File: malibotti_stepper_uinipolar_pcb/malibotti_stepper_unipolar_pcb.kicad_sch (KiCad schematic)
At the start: 34 parts, among them J1 Stepper 1, J2 Stepper 2, J3 Servo, J4 I2C, J5 USB_C_Receptacle_USB2.0_16P, J6 Serial, SW1 RST, SW2 MicroSwitchLeft, SW3 MicroSwitchRight, SW8 BTN, U1 TBD62783A, U3 AMS1117, U5 ESP32-S3-MINI-1

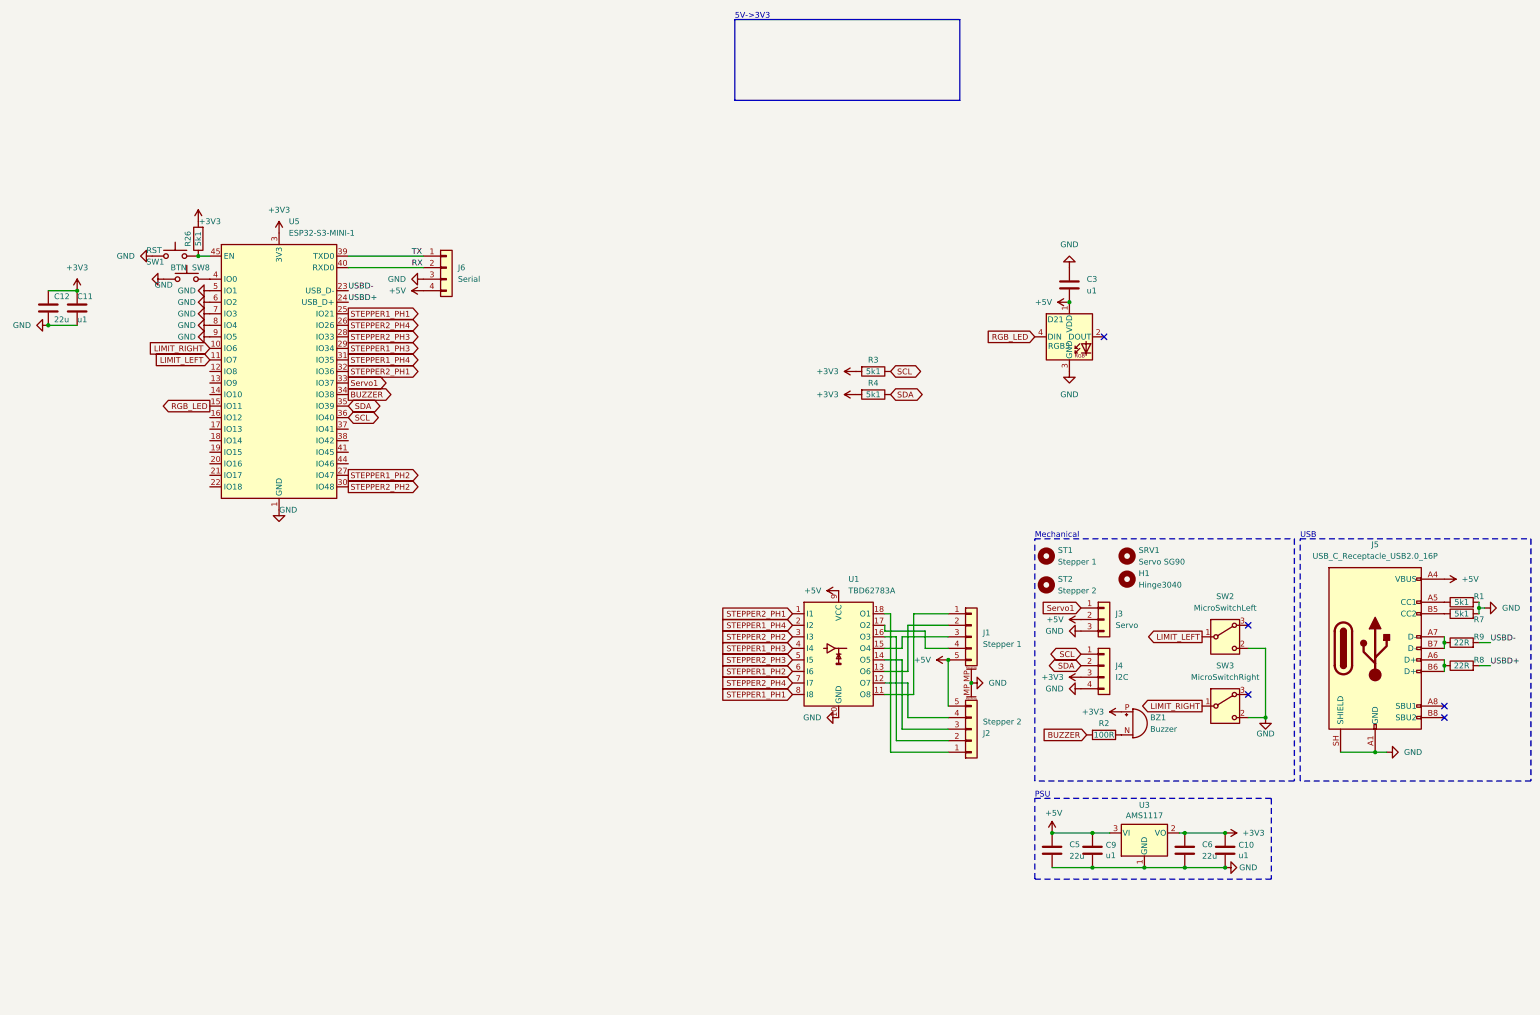
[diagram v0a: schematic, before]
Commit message: WebControlled Malibotti with working steppers
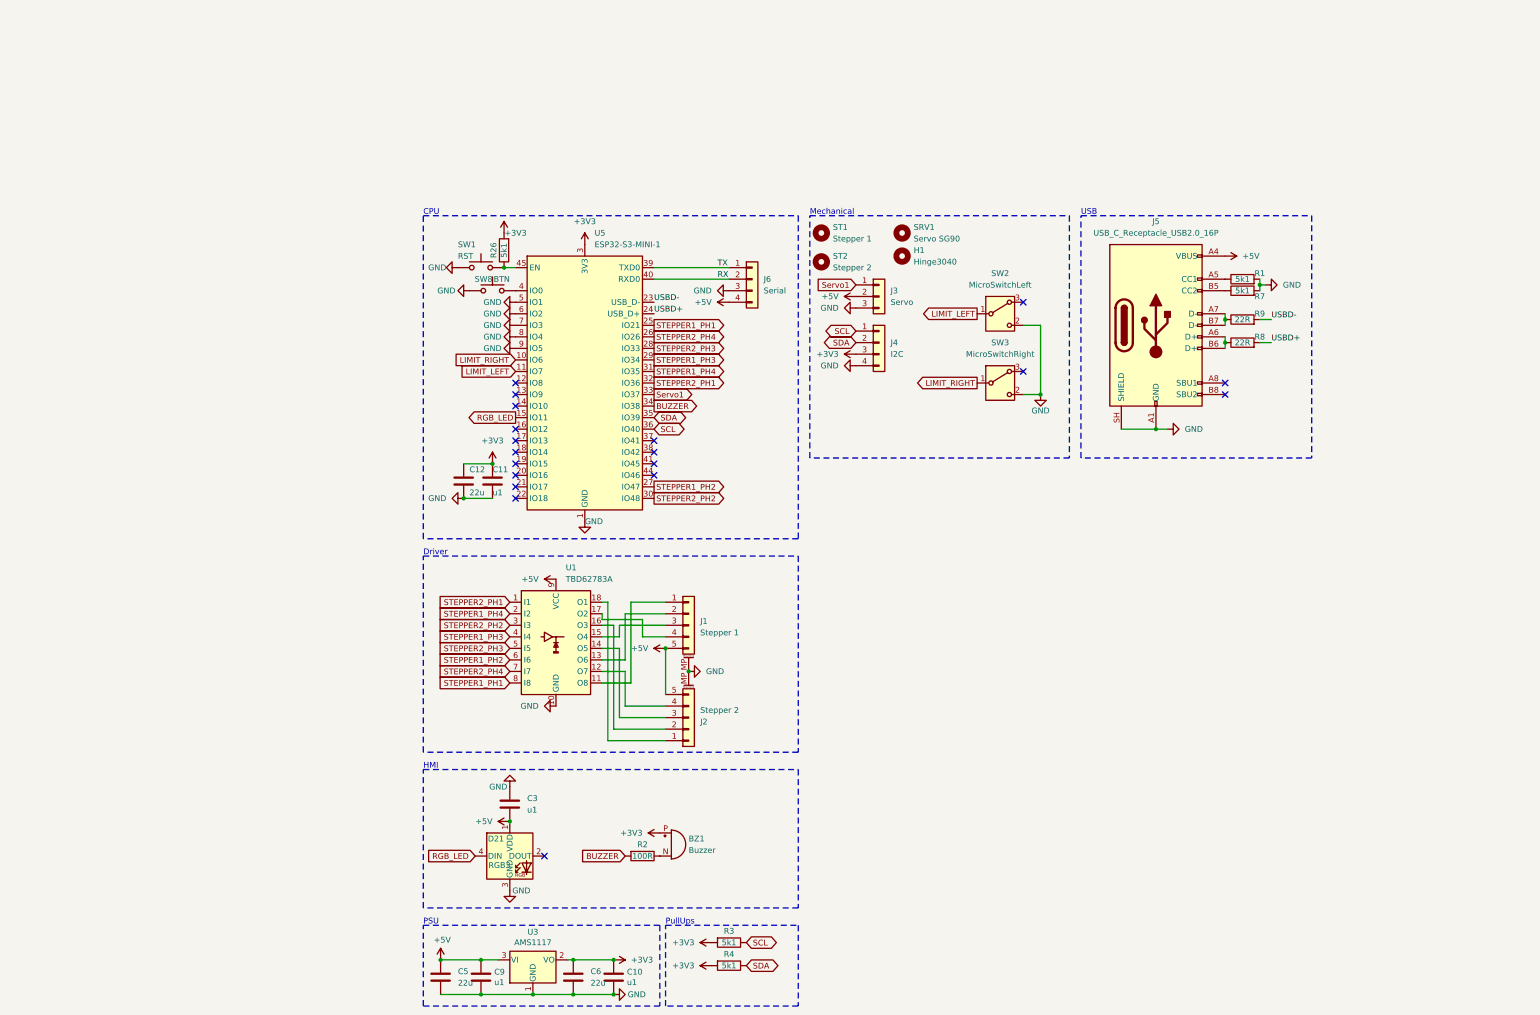
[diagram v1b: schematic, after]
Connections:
- no-connect marks 5 -> 19
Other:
- note added: "CPU"
- note added: "Driver"
- note added: "HMI"
- note added: "PullUps"
- note removed: "5V->3V3"
- moved on the sheet: BZ1, C10, C11, C12, C3, C5, C6, C9, D21, H1, J1, J2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

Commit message: Varions
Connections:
- net +5V: no longer J1.5 (Pin_5), J2.5 (Pin_5)
- net GND: now also J1.1 (Pin_1), J2.1 (Pin_1)
- net at U1.18 (O1): now also J2.5 (Pin_5); no longer J2.1 (Pin_1)
- net at J2.2 (Pin_2): now also U1.12 (O7); no longer U1.16 (O3)
- net at J2.4 (Pin_4): now also U1.16 (O3); no longer U1.12 (O7)
- net at U1.11 (O8): now also J1.5 (Pin_5); no longer J1.1 (Pin_1)
- net at U1.13 (O6): now also J1.4 (Pin_4); no longer J1.2 (Pin_2)
- net at U1.17 (O2): now also J1.2 (Pin_2); no longer J1.4 (Pin_4)
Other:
- moved on the sheet: J1
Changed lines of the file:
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@@
 	)
 	(junction
-		(at 67.31 110.49)
-		(diameter 0)
-		(color 0 0 0 0)
-	)
-	(junction
 		(at 33.02 148.59)
 		(diameter 0)
@@
 	)
 	(junction
-		(at 55.88 179.07)
+		(at 67.31 115.57)
 		(diameter 0)
 		(color 0 0 0 0)
 	)
 	(junction
-		(at 198.12 30.48)
+		(at 55.88 179.07)
 		(diameter 0)
 		(color 0 0 0 0)
 	)
 	(junction
-		(at 72.39 115.57)
+		(at 198.12 30.48)
 		(diameter 0)
 		(color 0 0 0 0)
@@
 	(wire
 		(pts
-			(xy 67.31 128.27) (xy 55.88 128.27)
+			(xy 67.31 124.46) (xy 55.88 124.46)
 		)
 		(stroke
@@
 	(wire
 		(pts
-			(xy 55.88 128.27) (xy 55.88 105.41)
+			(xy 55.88 124.46) (xy 55.88 105.41)
 		)
 		(stroke
@@
 	(wire
 		(pts
-			(xy 57.15 125.73) (xy 57.15 110.49)
+			(xy 57.15 121.92) (xy 57.15 110.49)
 		)
 		(stroke
@@
 	(wire
 		(pts
-			(xy 67.31 130.81) (xy 54.61 130.81)
+			(xy 67.31 127) (xy 54.61 127)
 		)
 		(stroke
@@
 	(wire
 		(pts
+			(xy 67.31 115.57) (xy 67.31 116.84)
+		)
+		(stroke
+			(width 0)
+			(type default)
+		)
+	)
+	(wire
+		(pts
 			(xy 58.42 102.87) (xy 58.42 113.03)
 		)
@@
 	(wire
 		(pts
-			(xy 54.61 130.81) (xy 54.61 100.33)
+			(xy 54.61 127) (xy 54.61 100.33)
 		)
 		(stroke
@@
 	(wire
 		(pts
-			(xy 67.31 110.49) (xy 67.31 120.65)
+			(xy 67.31 110.49) (xy 67.31 115.57)
 		)
 		(stroke
@@
 	(wire
 		(pts
-			(xy 58.42 123.19) (xy 58.42 115.57)
+			(xy 58.42 119.38) (xy 58.42 115.57)
 		)
 		(stroke
@@
 	(wire
 		(pts
-			(xy 67.31 125.73) (xy 57.15 125.73)
+			(xy 67.31 121.92) (xy 57.15 121.92)
 		)
 		(stroke
@@
 	(wire
 		(pts
-			(xy 67.31 123.19) (xy 58.42 123.19)
+			(xy 67.31 119.38) (xy 58.42 119.38)
 		)
 		(stroke
@@
 	)
 	(symbol
-		(lib_id "power:+5V")
-		(at 67.31 110.49 90)
-		(unit 1)
-		(body_style 1)
-		(exclude_from_sim no)
-		(in_bom yes)
-		(on_board yes)
-		(in_pos_files yes)
-		(dnp no)
-		(fields_autoplaced yes)
-		(property "Reference" "#PWR048"
-			(at 71.12 110.49 0)
-			(hide yes)
-			(show_name no)
-			(do_not_autoplace no)
-			(effects
-				(font
-					(size 1.27 1.27)
-				)
-			)
-		)
-		(property "Value" "+5V"
-			(at 63.5 110.4899 90)
-			(show_name no)
-			(do_not_autoplace no)
-			(effects
-				(font
-					(size 1.27 1.27)
-				)
-				(justify left)
-			)
-		)
-		(property "Footprint" ""
-			(at 67.31 110.49 0)
-			(hide yes)
-			(show_name no)
-			(do_not_autoplace no)
-			(effects
-				(font
-					(size 1.27 1.27)
-				)
-			)
-		)
-		(property "Datasheet" ""
-			(at 67.31 110.49 0)
-			(hide yes)
-			(show_name no)
-			(do_not_autoplace no)
-			(effects
-				(font
-					(size 1.27 1.27)
-				)
-			)
-		)
-		(property "Description" "Power symbol creates a global label with name \"+5V\""
-			(at 67.31 110.49 0)
-			(hide yes)
-			(show_name no)
-			(do_not_autoplace no)
-			(effects
-				(font
-					(size 1.27 1.27)
-				)
-			)
-		)
-		(pin "1"
-		)
-		(instances
-			(project "malibotti_stepper_unipolar_pcb"
-				(path "/e3c0928e-588c-4cab-a021-dc1d90fa1136"
-					(reference "#PWR048")
-					(unit 1)
-				)
-			)
-		)
-	)
-	(symbol
 		(lib_id "Connector_Generic:Conn_01x04")
 		(at 86.36 29.21 0)
@@
 	(symbol
 		(lib_id "Connector_Generic_MountingPin:Conn_01x05_MountingPin")
-		(at 72.39 125.73 0)
-		(mirror x)
+		(at 72.39 121.92 0)
 		(unit 1)
 		(body_style 1)
@@
 		(dnp no)
 		(property "Reference" "J2"
-			(at 74.93 126.6445 0)
+			(at 74.93 121.0055 0)
 			(show_name no)
 			(do_not_autoplace no)
@@
 		)
 		(property "Value" "Stepper 2"
-			(at 74.93 124.1045 0)
+			(at 74.93 123.5455 0)
 			(show_name no)
 			(do_not_autoplace no)
@@
 		)
 		(property "Footprint" "liebler_CONN:JST_XH_5P_SMD"
-			(at 72.39 125.73 0)
+			(at 72.39 121.92 0)
 			(hide yes)
 			(show_name no)
@@
 		)
 		(property "Datasheet" ""
-			(at 72.39 125.73 0)
+			(at 72.39 121.92 0)
 			(hide yes)
 			(show_name no)
@@
 		)
 		(property "Description" "Generic connectable mounting pin connector, single row, 01x05, script generated (kicad-library-utils/schlib/autogen/connector/)"
-			(at 72.39 125.73 0)
+			(at 72.39 121.92 0)
 			(hide yes)
 			(show_name no)
@@
 	)
 	(symbol
+		(lib_id "power:GND")
+		(at 72.39 132.08 90)
+		(unit 1)
+		(body_style 1)
+		(exclude_from_sim no)
+		(in_bom yes)
+		(on_board yes)
+		(in_pos_files yes)
+		(dnp no)
+		(fields_autoplaced yes)
+		(property "Reference" "#PWR053"
+			(at 78.74 132.08 0)
+			(hide yes)
+			(show_name no)
+			(do_not_autoplace no)
+			(effects
+				(font
+					(size 1.27 1.27)
+				)
+			)
+		)
+		(property "Value" "GND"
+			(at 76.2 132.0799 90)
+			(show_name no)
+			(do_not_autoplace no)
+			(effects
+				(font
+					(size 1.27 1.27)
+				)
+				(justify right)
+			)
+		)
+		(property "Footprint" ""
+			(at 72.39 132.08 0)
+			(hide yes)
+			(show_name no)
+			(do_not_autoplace no)
+			(effects
+				(font
+					(size 1.27 1.27)
+				)
+			)
+		)
+		(property "Datasheet" ""
+			(at 72.39 132.08 0)
+			(hide yes)
+			(show_name no)
+			(do_not_autoplace no)
+			(effects
+				(font
+					(size 1.27 1.27)
+				)
+			)
+		)
+		(property "Description" "Power symbol creates a global label with name \"GND\" , ground"
+			(at 72.39 132.08 0)
+			(hide yes)
+			(show_name no)
+			(do_not_autoplace no)
+			(effects
+				(font
+					(size 1.27 1.27)
+				)
+			)
+		)
+		(pin "1"
+		)
+		(instances
+			(project "malibotti_stepper_unipolar_pcb"
+				(path "/e3c0928e-588c-4cab-a021-dc1d90fa1136"
+					(reference "#PWR053")
+					(unit 1)
+				)
+			)
+		)
+	)
+	(symbol
 		(lib_id "Device:C")
 		(at 46.99 182.88 0)
@@
 		(lib_id "Connector_Generic_MountingPin:Conn_01x05_MountingPin")
 		(at 72.39 105.41 0)
+		(mirror x)
 		(unit 1)
 		(body_style 1)
@@
 		(in_pos_files yes)
 		(dnp no)
-		(fields_autoplaced yes)
 		(property "Reference" "J1"
-			(at 74.93 104.4955 0)
+			(at 74.93 106.3245 0)
 			(show_name no)
 			(do_not_autoplace no)
@@
 		)
 		(property "Value" "Stepper 1"
-			(at 74.93 107.0355 0)
+			(at 74.93 103.7845 0)
 			(show_name no)
 			(do_not_autoplace no)
@@
 	(symbol
 		(lib_id "power:GND")
+		(at 72.39 95.25 90)
+		(unit 1)
+		(body_style 1)
+		(exclude_from_sim no)
+		(in_bom yes)
+		(on_board yes)
+		(in_pos_files yes)
+		(dnp no)
+		(fields_autoplaced yes)
+		(property "Reference" "#PWR050"
+			(at 78.74 95.25 0)
+			(hide yes)
+			(show_name no)
+			(do_not_autoplace no)
+			(effects
+				(font
+					(size 1.27 1.27)
+				)
+			)
+		)
+		(property "Value" "GND"
+			(at 76.2 95.2499 90)
+			(show_name no)
+			(do_not_autoplace no)
+			(effects
+				(font
+					(size 1.27 1.27)
+				)
+				(justify right)
+			)
+		)
+		(property "Footprint" ""
+			(at 72.39 95.25 0)
+			(hide yes)
+			(show_name no)
+			(do_not_autoplace no)
+			(effects
+				(font
+					(size 1.27 1.27)
+				)
+			)
+		)
+		(property "Datasheet" ""
+			(at 72.39 95.25 0)
+			(hide yes)
+			(show_name no)
+			(do_not_autoplace no)
+			(effects
+				(font
+					(size 1.27 1.27)
+				)
+			)
+		)
+		(property "Description" "Power symbol creates a global label with name \"GND\" , ground"
+			(at 72.39 95.25 0)
+			(hide yes)
+			(show_name no)
+			(do_not_autoplace no)
+			(effects
+				(font
+					(size 1.27 1.27)
+				)
+			)
+		)
+		(pin "1"
+		)
+		(instances
+			(project "malibotti_stepper_unipolar_pcb"
+				(path "/e3c0928e-588c-4cab-a021-dc1d90fa1136"
+					(reference "#PWR050")
+					(unit 1)
+				)
+			)
+		)
+	)
+	(symbol
+		(lib_id "power:GND")
 		(at 21.59 26.67 270)
 		(unit 1)
@@
 	(symbol
 		(lib_id "power:GND")
-		(at 72.39 115.57 90)
+		(at 67.31 115.57 270)
 		(unit 1)
 		(body_style 1)
@@
 		(fields_autoplaced yes)
 		(property "Reference" "#PWR049"
-			(at 78.74 115.57 0)
+			(at 60.96 115.57 0)
 			(hide yes)
 			(show_name no)
@@
 		)
 		(property "Value" "GND"
-			(at 76.2 115.5699 90)
+			(at 66.04 111.76 90)
 			(show_name no)
 			(do_not_autoplace no)
@@
 					(size 1.27 1.27)
 				)
-				(justify right)
 			)
 		)
 		(property "Footprint" ""
-			(at 72.39 115.57 0)
+			(at 67.31 115.57 0)
 			(hide yes)
 			(show_name no)
@@
 		)
 		(property "Datasheet" ""
-			(at 72.39 115.57 0)
+			(at 67.31 115.57 0)
 			(hide yes)
 			(show_name no)
@@
 		)
 		(property "Description" "Power symbol creates a global label with name \"GND\" , ground"
-			(at 72.39 115.57 0)
+			(at 67.31 115.57 0)
 			(hide yes)
 			(show_name no)
